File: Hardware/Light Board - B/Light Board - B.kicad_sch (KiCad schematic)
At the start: 11 parts, among them J1 V+, J2 V-

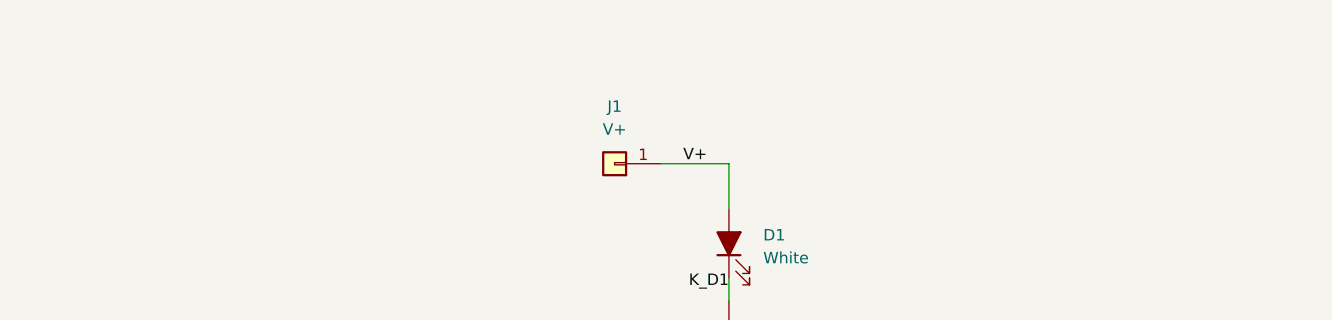
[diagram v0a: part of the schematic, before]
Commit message: Added note about incorrect footprint orientation
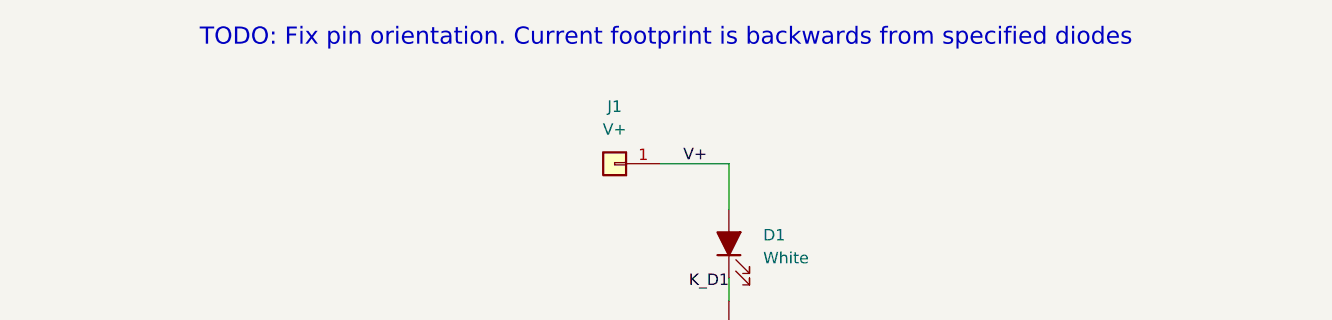
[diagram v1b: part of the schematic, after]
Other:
- note added: "TODO: Fix pin orientation. Current footprint is backwards from specified diodes"
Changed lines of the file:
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@@
 		(comment 1 "Isaac Rex")
+	)
+	(text "TODO: Fix pin orientation. Current footprint is backwards from specified diodes"
+		(exclude_from_sim no)
+		(at 106.045 64.77 0)
+		(effects
+			(font
+				(size 1.905 1.905)
+			)
+		)
 	)
 	(wire

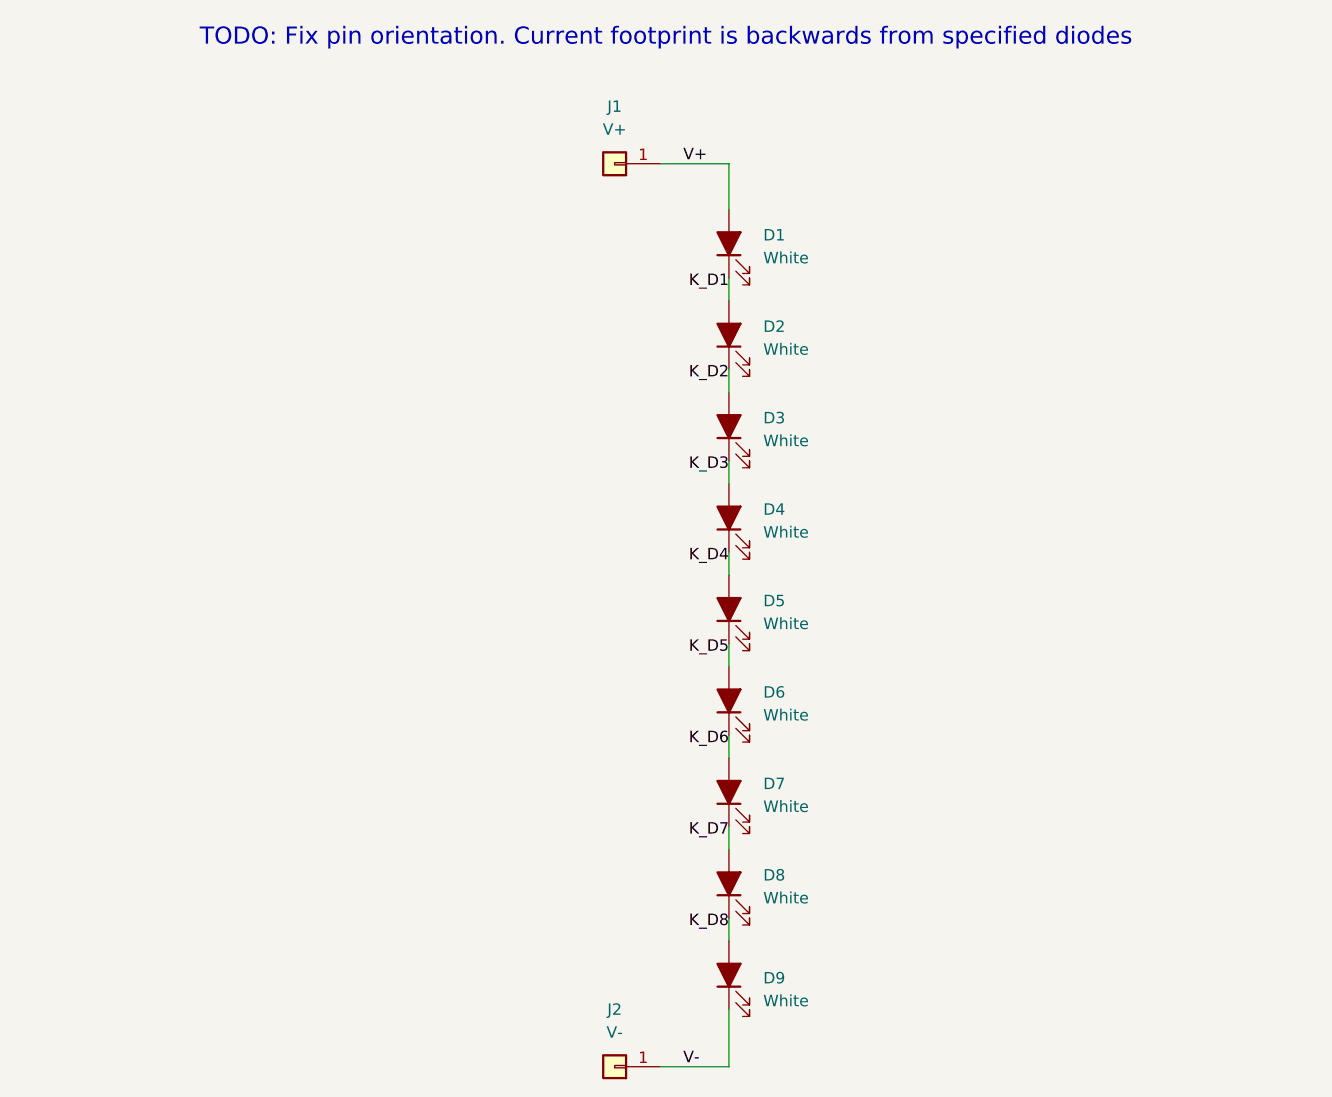
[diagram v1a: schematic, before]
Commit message: Added LED library and fixed orientation
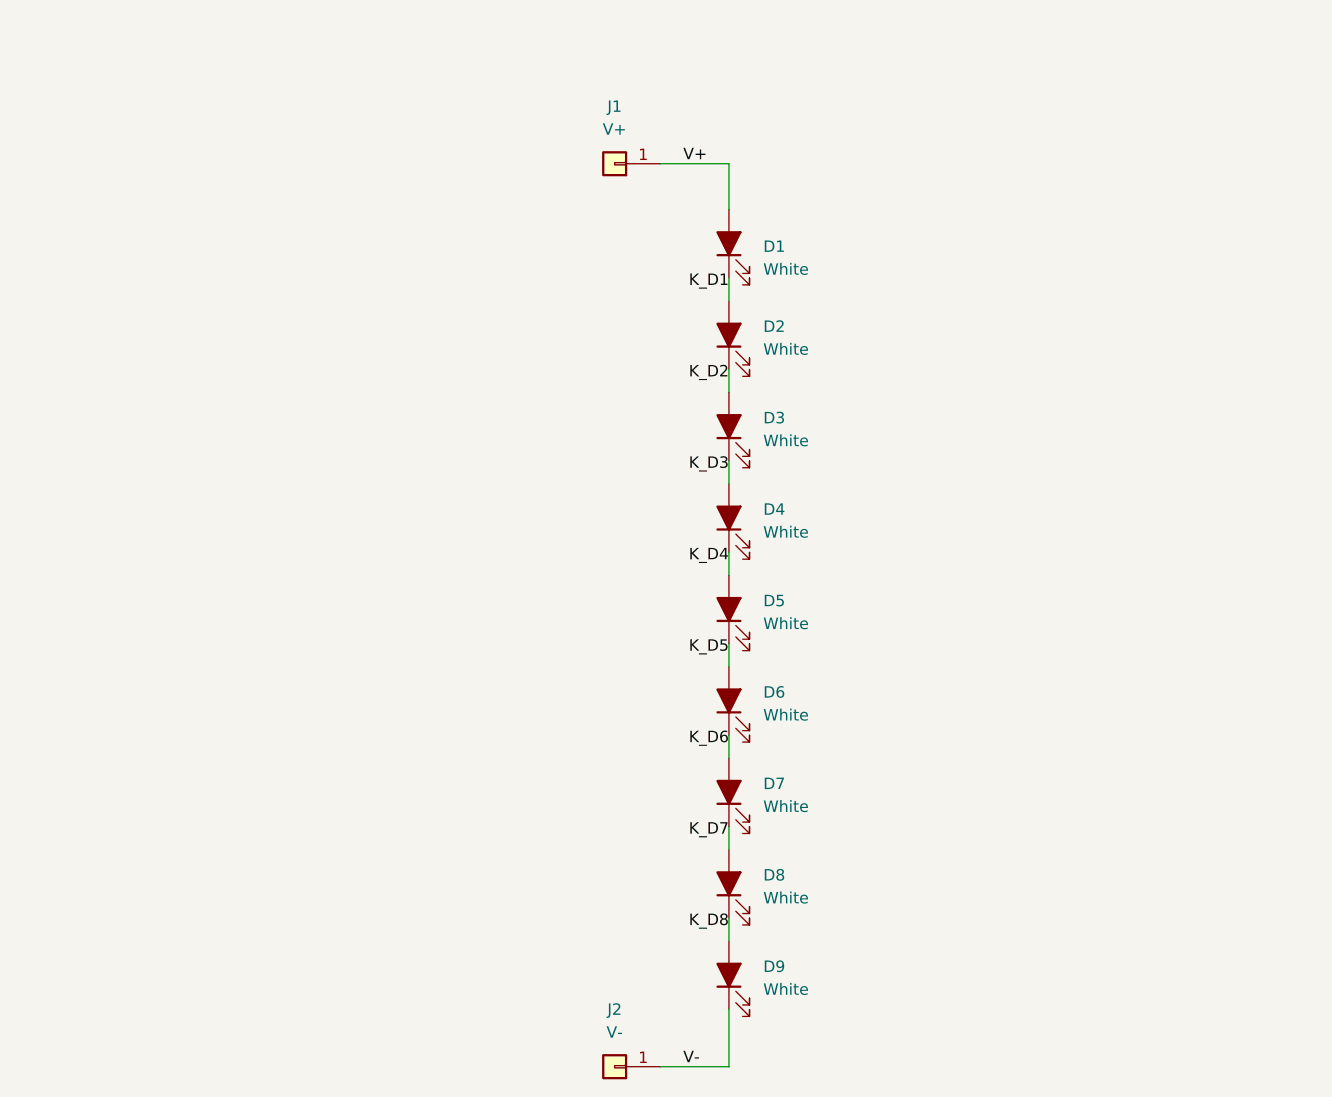
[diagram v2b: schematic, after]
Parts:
- D1: renamed from D9; footprint LED_SMD:LED_Everlight-SMD3528_3.5x2.8mm_67-21ST -> irex_LED_SMD:LED_Cree_J-Series_SMD2835_2.8x3.5mm
- D2: renamed from D8; footprint LED_SMD:LED_Everlight-SMD3528_3.5x2.8mm_67-21ST -> irex_LED_SMD:LED_Cree_J-Series_SMD2835_2.8x3.5mm
- D3: renamed from D7; footprint LED_SMD:LED_Everlight-SMD3528_3.5x2.8mm_67-21ST -> irex_LED_SMD:LED_Cree_J-Series_SMD2835_2.8x3.5mm
- D4: renamed from D6; footprint LED_SMD:LED_Everlight-SMD3528_3.5x2.8mm_67-21ST -> irex_LED_SMD:LED_Cree_J-Series_SMD2835_2.8x3.5mm
- D5: footprint LED_SMD:LED_Everlight-SMD3528_3.5x2.8mm_67-21ST -> irex_LED_SMD:LED_Cree_J-Series_SMD2835_2.8x3.5mm
- D6: renamed from D4; footprint LED_SMD:LED_Everlight-SMD3528_3.5x2.8mm_67-21ST -> irex_LED_SMD:LED_Cree_J-Series_SMD2835_2.8x3.5mm
- D7: renamed from D3; footprint LED_SMD:LED_Everlight-SMD3528_3.5x2.8mm_67-21ST -> irex_LED_SMD:LED_Cree_J-Series_SMD2835_2.8x3.5mm
- D8: renamed from D2; footprint LED_SMD:LED_Everlight-SMD3528_3.5x2.8mm_67-21ST -> irex_LED_SMD:LED_Cree_J-Series_SMD2835_2.8x3.5mm
- D9: renamed from D1; footprint LED_SMD:LED_Everlight-SMD3528_3.5x2.8mm_67-21ST -> irex_LED_SMD:LED_Cree_J-Series_SMD2835_2.8x3.5mm
- J1: renamed from J2; value V- -> V+
- J2: renamed from J1; value V+ -> V-
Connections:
- net K_D1: now also D1.1 (K), D2.2 (A); no longer D8.2 (A), D9.1 (K)
- net K_D2: now also D2.1 (K), D3.2 (A); no longer D7.2 (A), D8.1 (K)
- net K_D3: now also D3.1 (K), D4.2 (A); no longer D6.2 (A), D7.1 (K)
- net K_D4: now also D4.1 (K); no longer D6.1 (K)
- net K_D5: now also D6.2 (A); no longer D4.2 (A)
- net K_D6: now also D6.1 (K), D7.2 (A); no longer D3.2 (A), D4.1 (K)
- net K_D7: now also D7.1 (K), D8.2 (A); no longer D2.2 (A), D3.1 (K)
- net K_D8: now also D8.1 (K), D9.2 (A); no longer D1.2 (A), D2.1 (K)
- net V+: now also D1.2 (A), J1.1 (Pin_1); no longer D9.2 (A), J2.1 (Pin_1)
- net V-: now also D9.1 (K), J2.1 (Pin_1); no longer D1.1 (K), J1.1 (Pin_1)
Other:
- note removed: "TODO: Fix pin orientation. Current footprint is backwards from specified diodes"
- moved on the sheet: D1, D2, D3, D4, D6, D7, D8, D9, J1, J2
